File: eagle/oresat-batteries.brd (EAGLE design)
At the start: 94 x 93.5 mm, 65 parts, among them IC1 74AHC1G08DBV, U1 TCAN330, U2 STM32F042K6, X1 16MHz

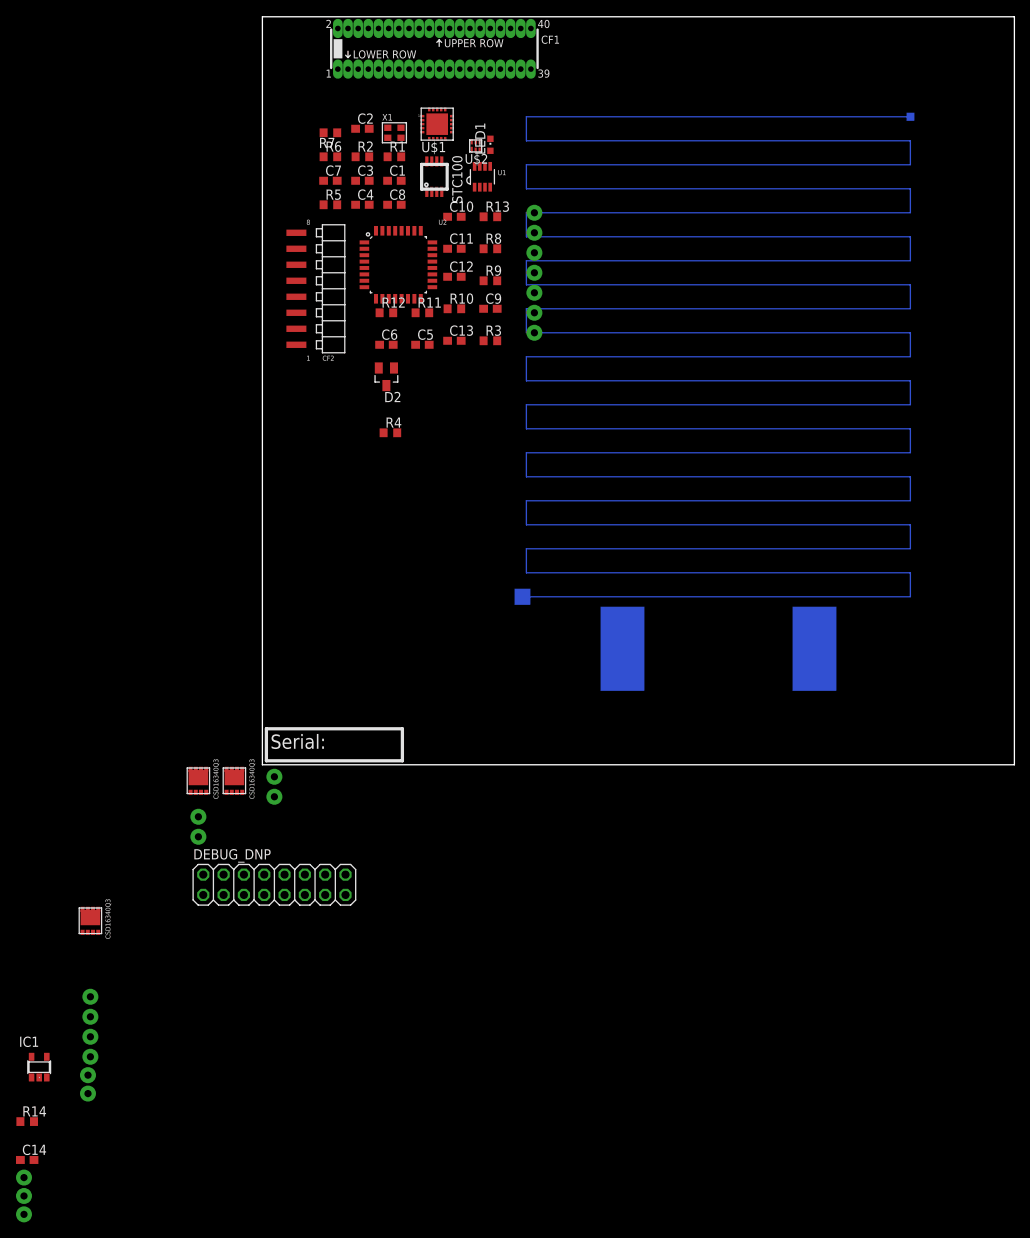
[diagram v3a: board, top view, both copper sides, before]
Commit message: Cleaned up schematic, added filter comp values
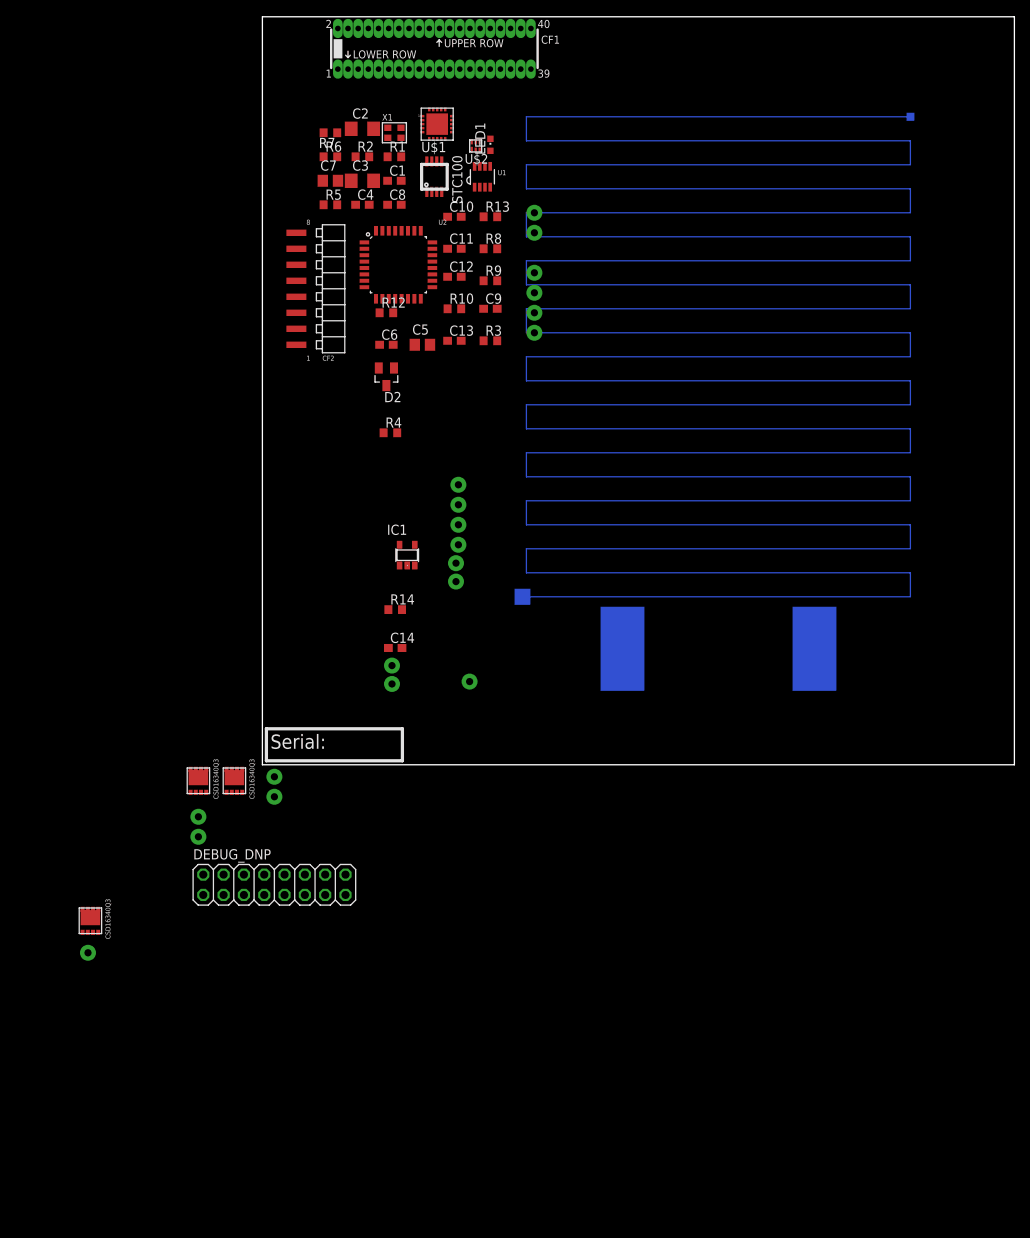
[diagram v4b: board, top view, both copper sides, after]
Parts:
- removed R11: (no value), rcl:R0603
- removed U$7: TP, oresat-batteries:2MM_TP
- added U$29: TP, oresat-batteries:2MM_TP
- C1: value (none) -> .1u
- C2, C3: value (none) -> 22u; device rcl:C0603 -> rcl:C1206
- C4: value (none) -> 100n
- C5: value (none) -> 10u; device rcl:C0603 -> rcl:C0805
- C6: value (none) -> .22u
- C7: value (none) -> 1u; device rcl:C0603 -> rcl:C0805
- R2: value (none) -> 220
- R5: value (none) -> 1k
- R7: value ? -> 330
- moved U$28 86.8 mm to (25.9, 10.4)
- moved C14 78.8 mm to (16.6, 14.6)
- moved IC1 78.8 mm to (18.1, 26.2)
- moved R14 78.8 mm to (16.6, 19.4)
- moved U$18 78.8 mm to (16.2, 12.4)
- moved U$19 78.8 mm to (16.2, 10.1)
- moved U$22 78.8 mm to (24.5, 35.0)
- moved U$23 78.8 mm to (24.5, 32.5)
- moved U$24 78.8 mm to (24.5, 30.0)
- moved U$25 78.8 mm to (24.5, 27.5)
- moved U$26 78.8 mm to (24.2, 25.2)
- moved U$27 78.8 mm to (24.2, 22.9)
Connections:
- removed net N$1: C7.2, R11.1, U$5.7
- net VBATT+: now also C7.2, U$29.P$1, U$5.7; no longer R11.2, U$7.P$1

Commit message: Added comp values
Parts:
- C14: value (none) -> .1u
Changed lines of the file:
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@@
 <element name="IC1" library="74xx-little-us" package="SOT23-5" value="74AHC1G08DBV" x="18.1" y="26.2"/>
 <element name="R14" library="rcl" package="R0603" value="2.2k" x="16.6" y="19.4"/>
-<element name="C14" library="rcl" package="C0603" value="" x="16.6" y="14.6"/>
+<element name="C14" library="rcl" package="C0603" value=".1u" x="16.6" y="14.6"/>
 <element name="U$18" library="oresat-batteries" package="2MM_TP" value="TP" x="16.2" y="12.4"/>
 <element name="U$19" library="oresat-batteries" package="2MM_TP" value="TP" x="16.2" y="10.1"/>

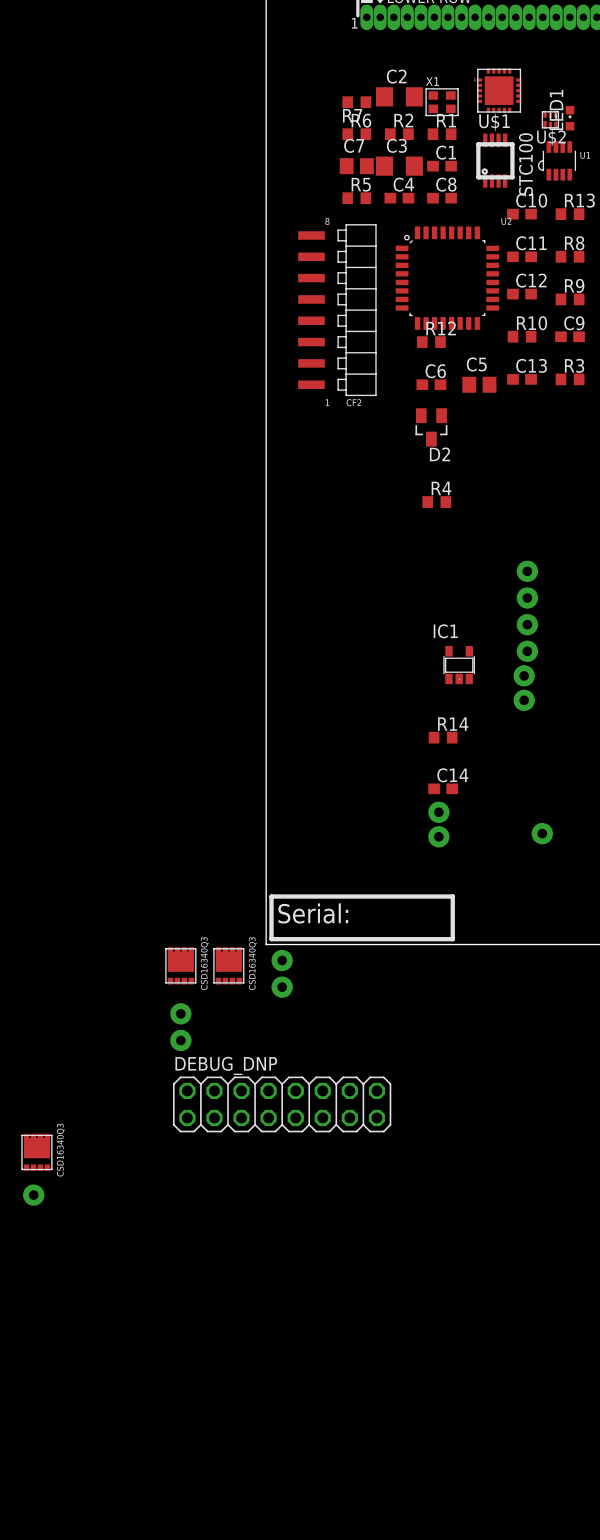
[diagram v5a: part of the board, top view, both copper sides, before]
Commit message: First battery board design review. Updated ADP symbol, package, and schematic.
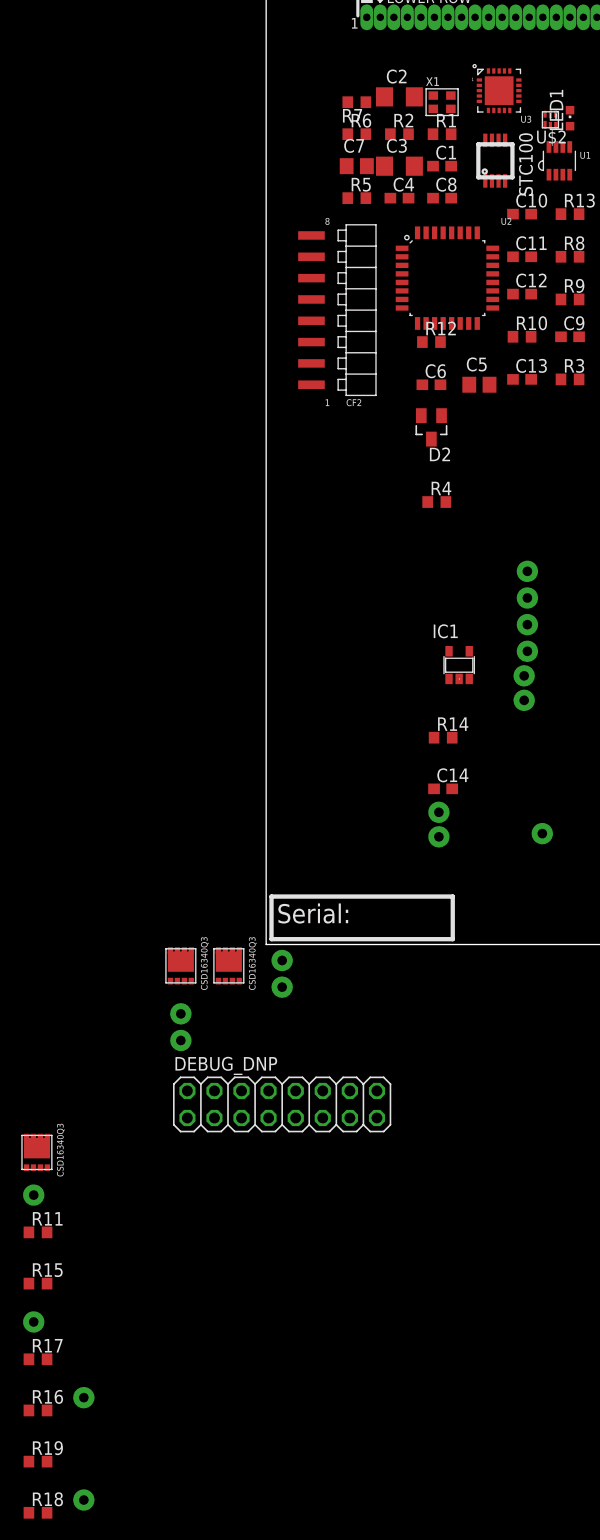
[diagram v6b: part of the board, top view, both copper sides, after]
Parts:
- added R11, R17, R18: 10k, rcl:R0603
- added R15, R19: DNP/10k, rcl:R0603
- added R16: DNP/10K, rcl:R0603
- added TP3, TP4, TP5: TP, oresat-batteries:2MM_TP
- C4: value 100n -> 10n
- LED1: value (none) -> DNP/GRN
- U3: value ADP5063 -> ADP5062
- renumbered U$1 to U3, U$24 to TP2, U$6 to TP1
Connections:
- new net 3V3: C10.1, C11.1, C12.1, C13.1, DEBUG_DNP.1, DEBUG_DNP.2, R10.2, R8.2, R9.2, U$15.P$1, U$20.P$5, U$20.P$6, U$20.P$7, U$20.P$8, U$20.P$9, U1.3, U2.1, U2.17, U2.5
- net DIG_IO1: now also R11.1, R15.2, TP3.P$1; no longer U2.15
- net DIG_IO2: now also R16.1, R17.2, TP4.P$1; no longer U2.26
- net DIG_IO3: now also R18.1, R19.2, TP5.P$1; no longer U2.27
- net GND: now also R15.1, R17.1, R19.1
- net VBATT+: no longer C10.1, C11.1, C12.1, C13.1, DEBUG_DNP.1, DEBUG_DNP.2, R10.2, R8.2, R9.2, U$15.P$1, U$20.P$5, U$20.P$6, U$20.P$7, U$20.P$8, U$20.P$9, U1.3, U2.1, U2.17, U2.5
- net VSOLAR: now also R11.2, R16.2, R18.2
